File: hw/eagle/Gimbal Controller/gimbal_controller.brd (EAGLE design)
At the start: 49.7 x 31.2 mm, 32 parts, among them X1 PROG, X3 22-23-2031, X4 MOTOR

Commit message: fixed some stuff
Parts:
- X2: value 22-23-2021 -> BATT
- X3: value 22-23-2031 -> UART
- renumbered BATT to X2
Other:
- board text added: "BATT"
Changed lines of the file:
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@@
 <text x="48.768" y="23.622" size="0.762" layer="21" rot="R90">LiPo 1Cell</text>
 <text x="25.654" y="11.43" size="1.016" layer="21" font="vector" rot="R45">PIC24FJ</text>
+<text x="47.244" y="23.622" size="1.016" layer="23" rot="R90">BATT</text>
 </plain>
 <attributes>
@@
 </autorouter>
 <elements>
-<element name="BATT" library="con-molex" package="22-23-2021" value="22-23-2021" x="44.45" y="25.908" smashed="yes" rot="R270">
+<element name="X2" library="con-molex" package="22-23-2021" value="BATT" x="44.45" y="25.908" smashed="yes" rot="R270">
 <attribute name="OC_FARNELL" value="1462926" x="44.45" y="25.908" size="1.778" layer="27" rot="R270" display="off"/>
 <attribute name="MPN" value="22-23-2021" x="44.45" y="25.908" size="1.778" layer="27" rot="R270" display="off"/>
 <attribute name="MF" value="MOLEX" x="44.45" y="25.908" size="1.778" layer="27" rot="R270" display="off"/>
 <attribute name="OC_NEWARK" value="25C3832" x="44.45" y="25.908" size="1.778" layer="27" rot="R270" display="off"/>
-<attribute name="NAME" x="47.244" y="23.622" size="1.016" layer="21" ratio="10" rot="R90"/>
 </element>
 <element name="C1" library="resistor" package="C0805" value="4.7u" x="39.116" y="23.241" smashed="yes" rot="R270">
@@
 <attribute name="NAME" x="26.924" y="25.654" size="1.27" layer="25" rot="R270"/>
 </element>
-<element name="X3" library="con-molex" package="22-23-2031" value="22-23-2031" x="5.334" y="26.924" smashed="yes" rot="R90">
+<element name="X3" library="con-molex" package="22-23-2031" value="UART" x="5.334" y="26.924" smashed="yes" rot="R90">
 <attribute name="OC_FARNELL" value="1462950" x="5.334" y="26.924" size="0.0508" layer="27" font="vector" rot="R90" display="off"/>
 <attribute name="MPN" value="22-23-2031" x="5.334" y="26.924" size="0.0508" layer="27" font="vector" rot="R90" display="off"/>
@@
 </element>
 <element name="U$8" library="power" package="SOT223" value="AP2114H-3.3AP2114H" x="33.274" y="24.638" smashed="yes" rot="R90">
-<attribute name="DIGIKEY-PARTNO" value="AP2114H-3.3TRG1DICT-ND" x="33.274" y="24.638" size="1.778" layer="27" rot="R90" display="off"/>
+<attribute name="DIGIKEY_PARTNO" value="AP2114H-3.3TRG1DICT-ND" x="33.274" y="24.638" size="1.778" layer="27" rot="R90" display="off"/>
 </element>
 <element name="U$7" library="mcu" package="TQFP64-10X10" value="PIC24FJ256GB406PIC24FJ256GB406" x="28.956" y="12.192" smashed="yes" rot="R45">
@@
 </signal>
 <signal name="VCC">
-<contactref element="BATT" pad="1"/>
+<contactref element="X2" pad="1"/>
 <contactref element="R10" pad="2"/>
 <contactref element="C2" pad="1"/>
@@
 </signal>
 <signal name="GND">
-<contactref element="BATT" pad="2"/>
+<contactref element="X2" pad="2"/>
 <contactref element="C3" pad="2"/>
 <contactref element="C4" pad="2"/>

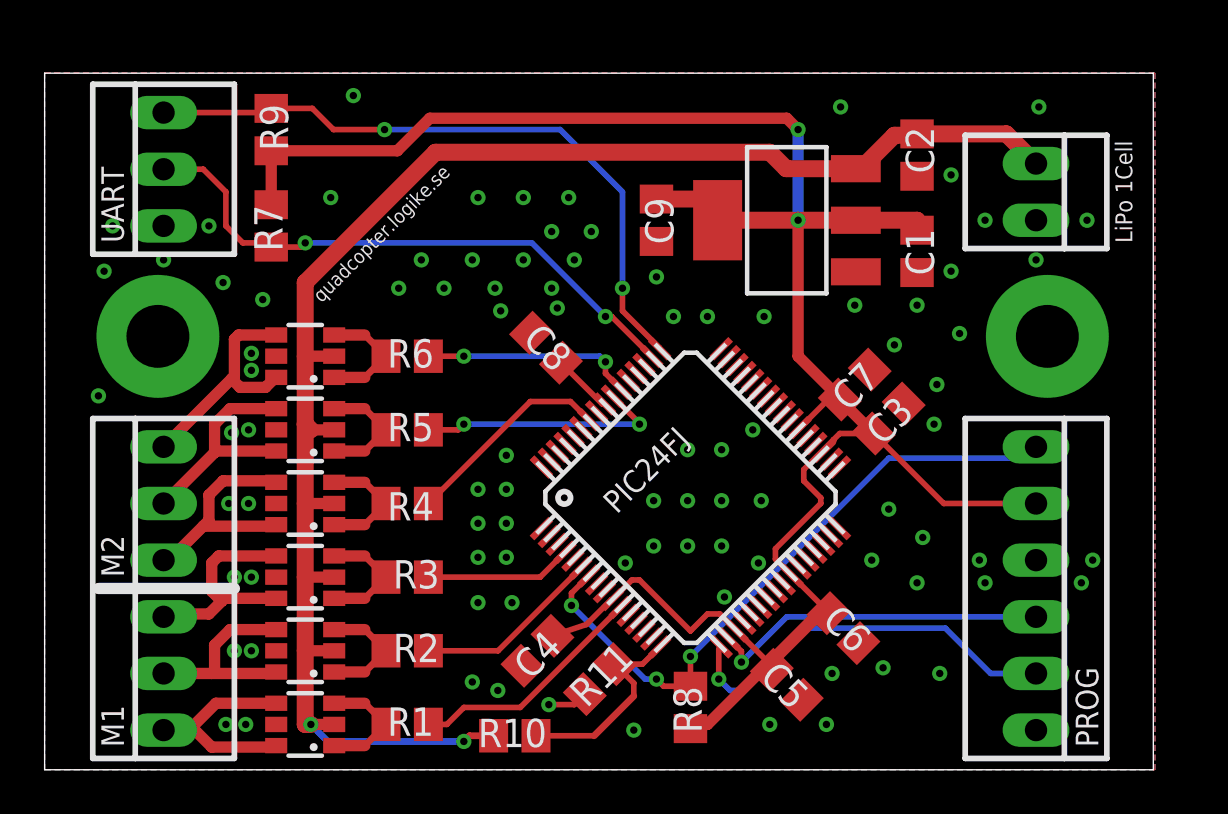
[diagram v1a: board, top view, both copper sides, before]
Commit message: added lt spice simulation
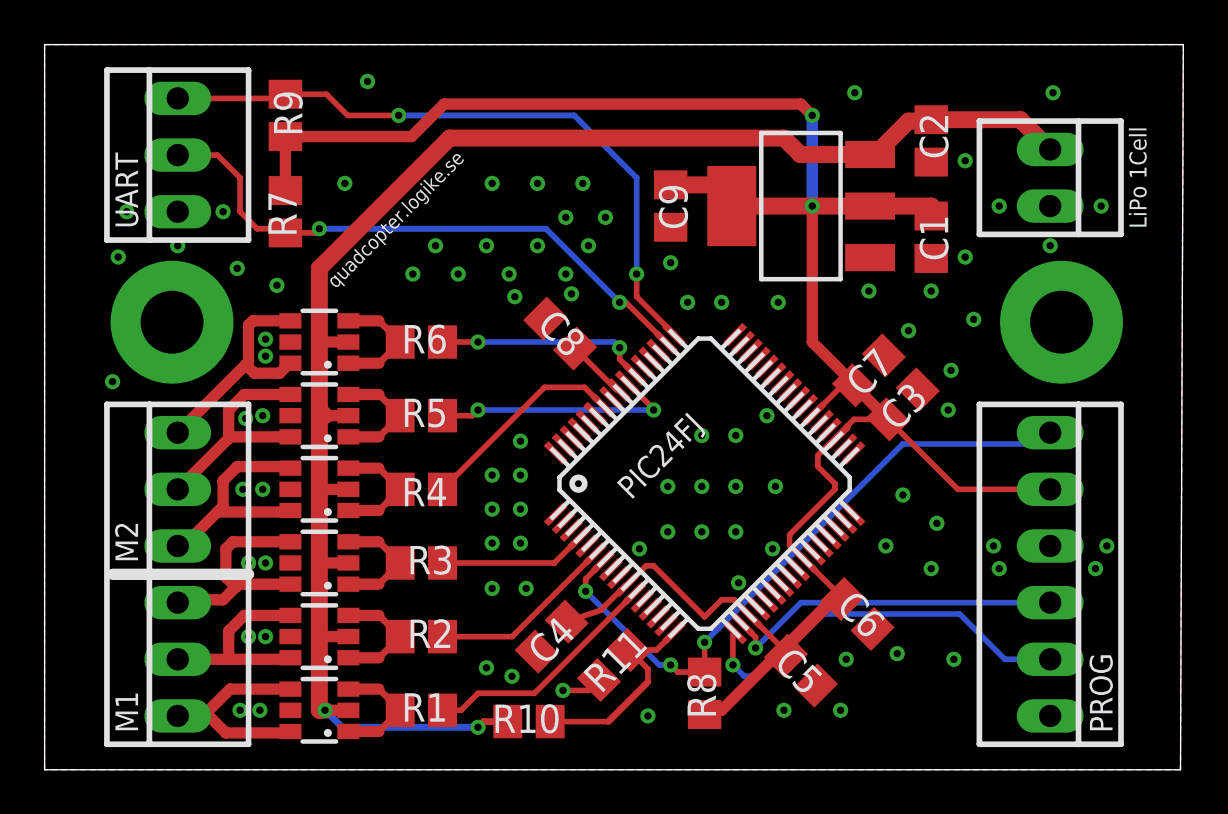
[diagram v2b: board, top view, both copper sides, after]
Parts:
- moved C3 0.90 mm to (38.5, 16.4)
- moved C8 0.90 mm to (23.1, 19.6)
- moved U$3 0.90 mm to (12.3, 9.27)
- moved C4 0.90 mm to (22.7, 5.97)
- moved U$2 0.90 mm to (12.3, 5.97)
- moved X3 0.90 mm to (5.97, 27.6)
- moved R11 0.90 mm to (25.5, 4.70)
- moved R8 0.90 mm to (29.6, 3.43)
- moved U$1 0.90 mm to (12.3, 2.67)
- moved U$4 0.90 mm to (12.3, 12.6)
- moved U$5 0.90 mm to (12.3, 15.9)
- moved U$7 0.90 mm to (29.6, 12.8)
- moved X4 0.90 mm to (5.97, 8.76)
- moved C1 0.90 mm to (39.8, 23.9)
- moved C7 0.90 mm to (37.0, 17.9)
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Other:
- board size 49.7 x 31.2 mm -> 51.1 x 32.5 mm

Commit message: minor fixes
- increased drill hole size on connectors
- changed all text to stop layer instead of overlay, so that the text
is seen in gold
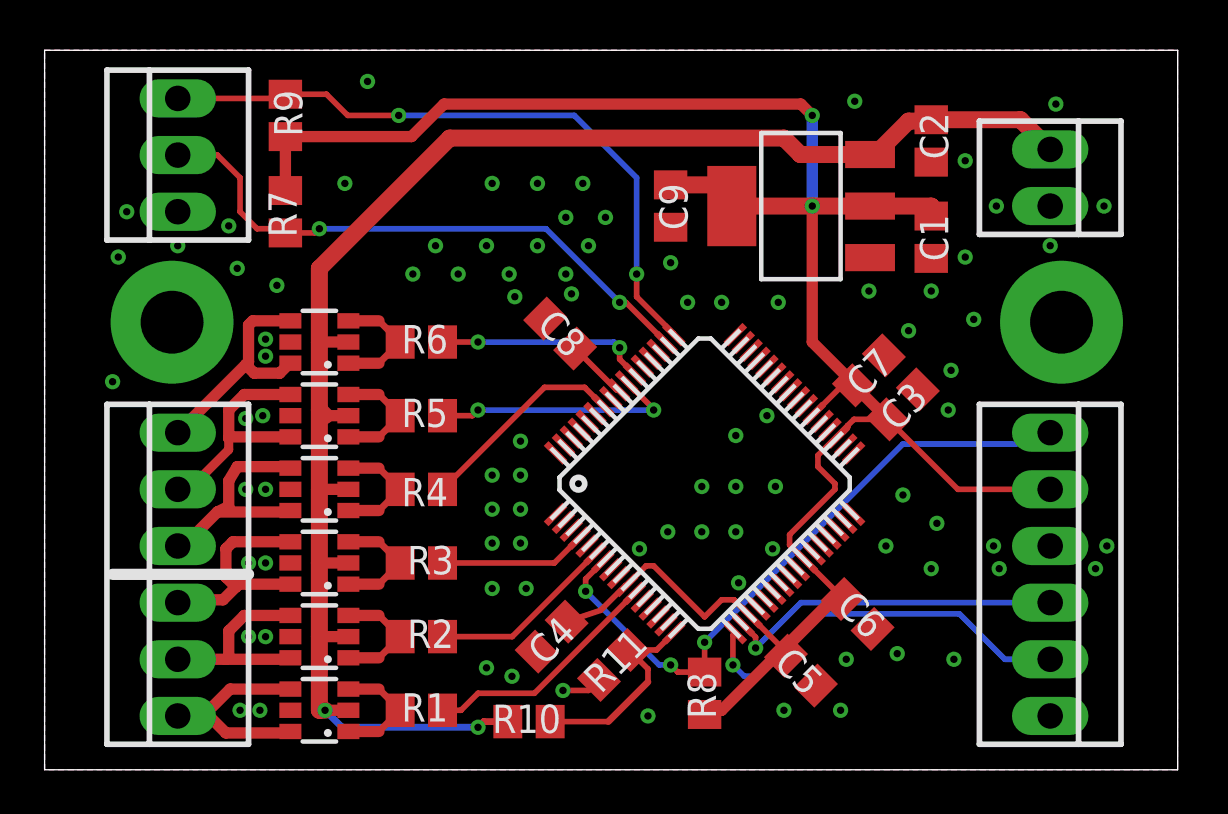
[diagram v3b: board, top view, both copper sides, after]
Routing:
- net GND: vias 92 -> 90
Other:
- board size 51.1 x 32.5 mm -> 50.8 x 32.3 mm
- board text added: "QG1624"
- board text added: "www.quadcopter.logike.se"
- board text removed: "LiPo 1Cell"
- board text removed: "QG1604"
- board text removed: "quadcopter.logike.se"
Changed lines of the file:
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@@
 <board>
 <plain>
-<wire x1="0" y1="0" x2="50.927" y2="0" width="0" layer="20"/>
-<wire x1="50.927" y1="0" x2="51.054" y2="32.512" width="0" layer="20"/>
-<wire x1="51.054" y1="32.512" x2="0" y2="32.512" width="0" layer="20"/>
-<wire x1="0" y1="32.512" x2="0" y2="0" width="0" layer="20"/>
-<text x="4.191" y="9.271" size="1.016" layer="21" rot="R90">M2</text>
-<text x="4.191" y="1.651" size="1.016" layer="21" rot="R90">M1</text>
-<text x="4.191" y="24.257" size="1.016" layer="21" rot="R90">UART</text>
-<text x="47.879" y="1.651" size="1.016" layer="21" rot="R90">PROG</text>
-<text x="42.926" y="2.54" size="1.016" layer="22" rot="MR0">QG1604</text>
-<text x="18.415" y="27.813" size="0.635" layer="21" rot="R225">quadcopter.logike.se</text>
+<wire x1="0" y1="0" x2="50.8" y2="0" width="0" layer="20"/>
+<wire x1="50.8" y1="0" x2="50.8" y2="32.258" width="0" layer="20"/>
+<wire x1="50.8" y1="32.258" x2="0" y2="32.258" width="0" layer="20"/>
+<wire x1="0" y1="32.258" x2="0" y2="0" width="0" layer="20"/>
+<text x="2.159" y="11.557" size="1.016" layer="29" rot="R90">M2</text>
+<text x="2.159" y="3.937" size="1.016" layer="29" rot="R90">M1</text>
+<text x="2.159" y="25.781" size="1.016" layer="29" rot="R90">UART</text>
+<text x="49.911" y="7.239" size="1.016" layer="29" rot="R90">PROG</text>
 <wire x1="3.048" y1="8.763" x2="9.144" y2="8.763" width="0.508" layer="21"/>
-<text x="49.403" y="24.257" size="0.762" layer="21" rot="R90">LiPo 1Cell</text>
-<text x="26.289" y="12.065" size="1.016" layer="21" font="vector" rot="R45">PIC24FJ</text>
-<text x="47.879" y="24.257" size="1.016" layer="23" rot="R90">BATT</text>
+<text x="26.289" y="12.065" size="1.016" layer="29" font="vector" rot="R45">PIC24FJ</text>
+<text x="49.911" y="24.765" size="1.016" layer="29" rot="R90">BATT</text>
+<text x="50.038" y="31.623" size="1.016" layer="29" rot="R180">www.quadcopter.logike.se</text>
+<text x="49.022" y="1.143" size="1.016" layer="30" rot="MR90">QG1624</text>
 </plain>
 <attributes>
@@
 <wire x1="5.969" y1="10.033" x2="6.223" y2="10.033" width="0.508" layer="1"/>
 <wire x1="6.223" y1="10.033" x2="7.747" y2="11.557" width="0.508" layer="1"/>
-<wire x1="7.747" y1="11.557" x2="8.001" y2="11.811" width="0.508" layer="1"/>
-<wire x1="8.001" y1="11.811" x2="8.001" y2="12.954" width="0.508" layer="1"/>
-<wire x1="8.001" y1="12.954" x2="8.636" y2="13.589" width="0.508" layer="1"/>
+<wire x1="7.747" y1="11.557" x2="8.255" y2="11.811" width="0.508" layer="1"/>
+<wire x1="8.255" y1="11.811" x2="8.255" y2="12.954" width="0.508" layer="1"/>
+<wire x1="8.255" y1="12.954" x2="8.636" y2="13.589" width="0.508" layer="1"/>
 <wire x1="8.636" y1="13.589" x2="10.953" y2="13.589" width="0.508" layer="1"/>
 <contactref element="U$4" pad="6"/>
@@
 <contactref element="X1" pad="3"/>
 <polygon width="0.1524" layer="1">
-<vertex x="0" y="32.512"/>
-<vertex x="51.054" y="32.512"/>
-<vertex x="50.927" y="0"/>
+<vertex x="0" y="32.258"/>
+<vertex x="50.8" y="32.258"/>
+<vertex x="50.8" y="0"/>
 <vertex x="0" y="0"/>
 </polygon>
 <polygon width="0.1524" layer="16">
-<vertex x="0" y="32.512"/>
-<vertex x="51.054" y="32.512"/>
-<vertex x="50.927" y="0"/>
+<vertex x="0" y="32.258"/>
+<vertex x="50.8" y="32.258"/>
+<vertex x="50.8" y="0"/>
 <vertex x="0" y="0"/>
 </polygon>
@@
 <via x="9.017" y="15.748" extent="1-16" drill="0.3302" diameter="0.3048"/>
 <via x="9.779" y="15.875" extent="1-16" drill="0.3302" diameter="0.3048"/>
-<via x="8.89" y="12.573" extent="1-16" drill="0.3302" diameter="0.3048"/>
-<via x="9.779" y="12.573" extent="1-16" drill="0.3302" diameter="0.3048"/>
+<via x="9.017" y="12.573" extent="1-16" drill="0.3302" diameter="0.3048"/>
+<via x="9.906" y="12.573" extent="1-16" drill="0.3302" diameter="0.3048"/>
 <via x="8.763" y="2.667" extent="1-16" drill="0.3302" diameter="0.3048"/>
 <via x="9.652" y="2.667" extent="1-16" drill="0.3302" diameter="0.3048"/>
@@
 <contactref element="X3" pad="1"/>
 <via x="3.683" y="25.019" extent="1-16" drill="0.3302" diameter="0.3048"/>
-<via x="8.001" y="25.019" extent="1-16" drill="0.3302" diameter="0.3048"/>
+<via x="8.255" y="24.384" extent="1-16" drill="0.3302" diameter="0.3048"/>
 <via x="5.969" y="23.495" extent="1-16" drill="0.3302" diameter="0.3048"/>
 <via x="28.067" y="22.733" extent="1-16" drill="0.3302" diameter="0.3048"/>
@@
 <via x="41.275" y="22.987" extent="1-16" drill="0.3302" diameter="0.3048"/>
 <via x="41.275" y="27.305" extent="1-16" drill="0.3302" diameter="0.3048"/>
-<via x="42.799" y="25.273" extent="1-16" drill="0.3302" diameter="0.3048"/>
+<via x="42.672" y="25.273" extent="1-16" drill="0.3302" diameter="0.3048"/>
 <via x="45.085" y="23.495" extent="1-16" drill="0.3302" diameter="0.3048"/>
-<via x="47.371" y="25.273" extent="1-16" drill="0.3302" diameter="0.3048"/>
+<via x="47.498" y="25.273" extent="1-16" drill="0.3302" diameter="0.3048"/>
 <via x="20.066" y="26.289" extent="1-16" drill="0.3302"/>
 <via x="22.098" y="26.289" extent="1-16" drill="0.3302"/>
@@
 <via x="29.464" y="12.7" extent="1-16" drill="0.3302"/>
 <via x="30.988" y="14.986" extent="1-16" drill="0.3302"/>
-<via x="29.464" y="14.986" extent="1-16" drill="0.3302"/>
 <via x="30.988" y="12.7" extent="1-16" drill="0.3302"/>
-<via x="27.94" y="12.7" extent="1-16" drill="0.3302"/>
 <via x="27.94" y="10.668" extent="1-16" drill="0.3302"/>
 <via x="29.464" y="10.668" extent="1-16" drill="0.3302"/>
@@
 <via x="3.048" y="17.399" extent="1-16" drill="0.3302"/>
 <via x="13.462" y="26.289" extent="1-16" drill="0.3302"/>
-<via x="36.322" y="30.353" extent="1-16" drill="0.3302"/>
-<via x="45.212" y="30.353" extent="1-16" drill="0.3302"/>
+<via x="36.322" y="29.972" extent="1-16" drill="0.3302"/>
+<via x="45.339" y="29.845" extent="1-16" drill="0.3302"/>
 <via x="41.656" y="20.193" extent="1-16" drill="0.3302"/>
 <via x="38.481" y="12.319" extent="1-16" drill="0.3302"/>
@@
 <wire x1="8.951" y1="16.825" x2="8.255" y2="16.129" width="0.508" layer="1"/>
 <wire x1="8.255" y1="16.129" x2="8.255" y2="14.859" width="0.508" layer="1"/>
-<wire x1="8.255" y1="14.859" x2="5.969" y2="12.573" width="0.508" layer="1"/>
 <wire x1="8.321" y1="14.925" x2="8.255" y2="14.859" width="0.508" layer="1"/>
 <contactref element="U$5" pad="6"/>
@@
 <wire x1="8.951" y1="16.825" x2="11.019" y2="16.825" width="0.508" layer="1"/>
 <wire x1="11.019" y1="14.925" x2="8.321" y2="14.925" width="0.508" layer="1"/>
+<wire x1="8.255" y1="14.859" x2="8.255" y2="14.351" width="0.4064" layer="1"/>
+<wire x1="8.255" y1="14.351" x2="6.604" y2="12.7" width="0.4064" layer="1"/>
+<wire x1="6.604" y1="12.7" x2="6.096" y2="12.7" width="0.4064" layer="1"/>
+<wire x1="6.096" y1="12.7" x2="5.969" y2="12.573" width="0.4064" layer="1"/>
 </signal>
 <signal name="M2G2">

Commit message: added some pic24 code
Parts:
- R10: value 1.54k -> 470
- R11, R7, R9: value 2k -> 2.2k
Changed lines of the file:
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@@
 <attribute name="VALUE" x="40.005" y="16.383" size="1.016" layer="27" ratio="10" rot="R270"/>
 </element>
-<element name="R7" library="resistor" package="R0805" value="2k" x="10.795" y="25.019" smashed="yes" rot="R90">
+<element name="R7" library="resistor" package="R0805" value="2.2k" x="10.795" y="25.019" smashed="yes" rot="R90">
 <attribute name="NAME" x="11.303" y="23.876" size="1.27" layer="25" rot="R90"/>
 </element>
-<element name="R9" library="resistor" package="R0805" value="2k" x="10.795" y="29.337" smashed="yes" rot="R270">
+<element name="R9" library="resistor" package="R0805" value="2.2k" x="10.795" y="29.337" smashed="yes" rot="R270">
 <attribute name="NAME" x="10.287" y="30.48" size="1.27" layer="25" rot="R270"/>
 </element>
-<element name="R10" library="resistor" package="R0805" value="1.54k" x="21.717" y="2.159" smashed="yes" rot="R180">
+<element name="R10" library="resistor" package="R0805" value="470" x="21.717" y="2.159" smashed="yes" rot="R180">
 <attribute name="NAME" x="20.066" y="1.651" size="1.27" layer="25"/>
 </element>
-<element name="R11" library="resistor" package="R0805" value="2k" x="25.527" y="4.699" smashed="yes" rot="R45">
+<element name="R11" library="resistor" package="R0805" value="2.2k" x="25.527" y="4.699" smashed="yes" rot="R45">
 <attribute name="NAME" x="24.941959375" y="3.3700125" size="1.27" layer="25" rot="R45"/>
 </element>
